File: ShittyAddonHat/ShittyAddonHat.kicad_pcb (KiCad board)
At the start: 2 copper layers, 9 parts

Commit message: just before silk change
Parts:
- added ?: , RPi_Hat:RPi_Hat_Mounting_Hole, F.Cu at (210.0, 52.5)
- added ?: , RPi_Hat:RPi_Hat_Mounting_Hole, F.Cu at (210.0, 101.5)
- added ?: , RPi_Hat:RPi_Hat_Mounting_Hole, F.Cu at (152.0, 101.5)
- added ?: , RPi_Hat:RPi_Hat_Mounting_Hole, F.Cu at (152.0, 52.5)

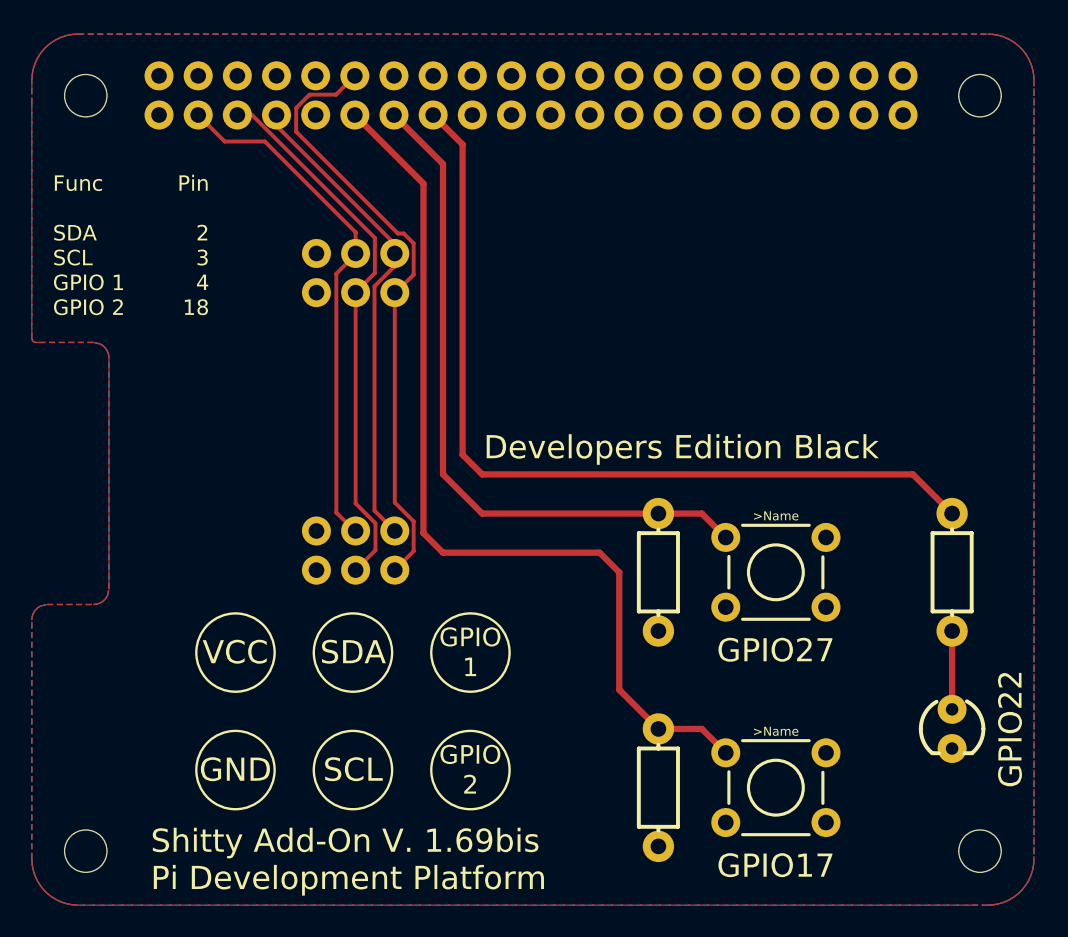
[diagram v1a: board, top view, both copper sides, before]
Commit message: mk2 run 1 changes, furshur
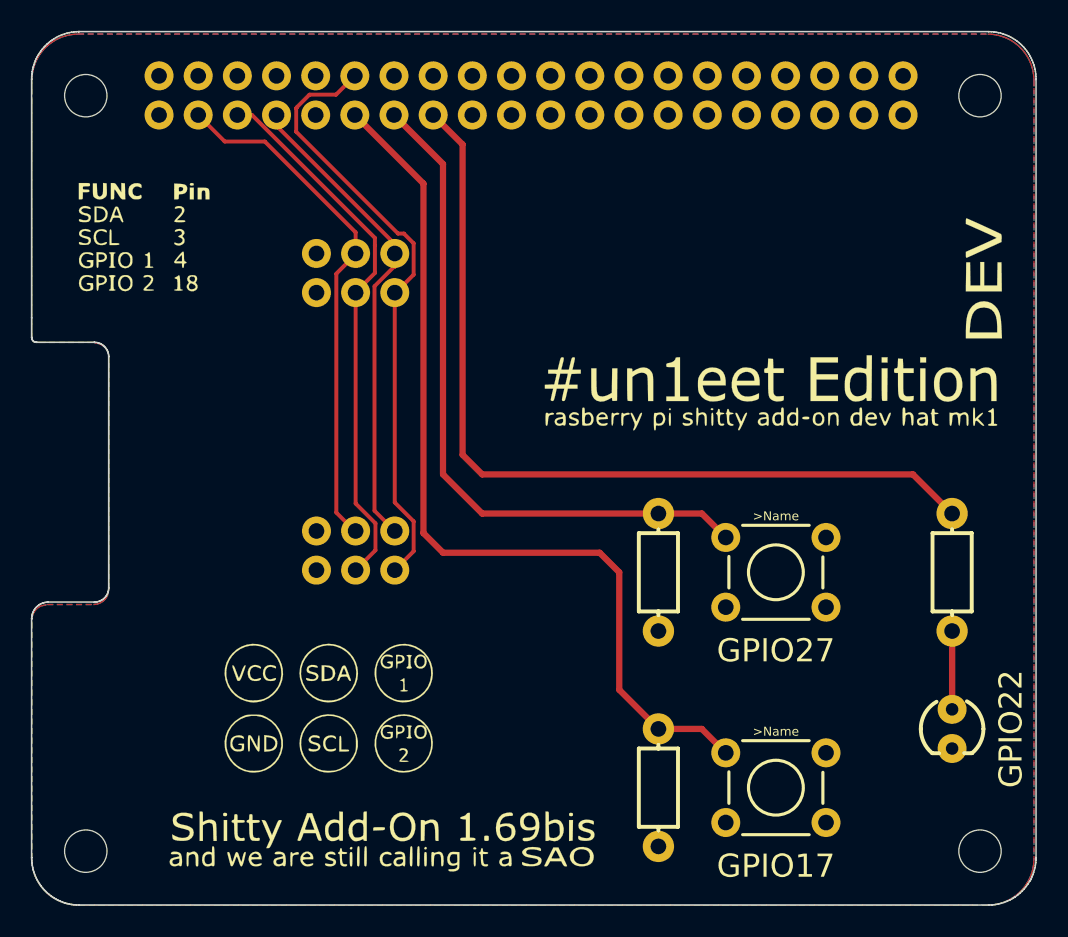
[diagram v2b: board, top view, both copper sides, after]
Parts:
- added ?: , mySAOhat:F.Silk_g8169, F.Cu at (181.6, 76.2)
- added ?: , mySAOhat:F.Mask_g8167, F.Cu at (181.6, 76.2)
- added ?: , mySAOhat:B.Mask_g8161, F.Cu at (177.8, 78.7)
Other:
- board outline added: 65.1 x 56.7 mm
- board text removed: "Developers Edition Black"
- board text removed: "Func SDA SCL GPIO 1 GPIO 2"
- board text removed: "GND"
- board text removed: "GPIO 1"
- board text removed: "GPIO 2"
- board text removed: "Pin 2 3 4 18"
- board text removed: "SCL"
- board text removed: "SDA"
- board text removed: "Shitty Add-On V. 1.69bis Pi Development Platform"
- board text removed: "VCC"
